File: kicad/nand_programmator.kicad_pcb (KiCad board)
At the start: 2 copper layers, 48 x 41 mm, 42 parts, among them J1 Conn_01x04, J2 Conn_01x03, J3 Conn_02x12_Odd_Even_Left, J4 Conn_02x12_Odd_Even_Right, J5 BOOT0, J6 ~RST, P1 USB, U1 LM1117-3.3, U2 STM32F103VCT6, Y1 Crystal_SMD_8MHz_18pF

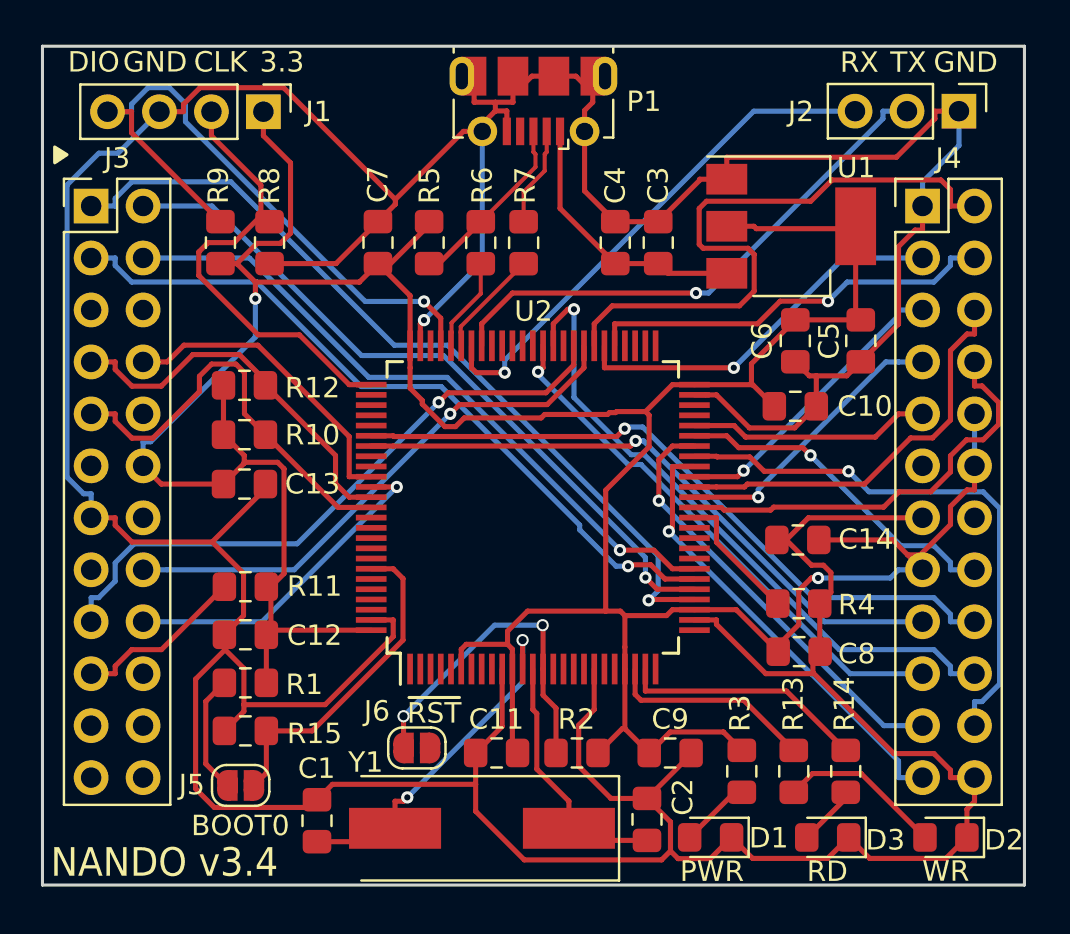
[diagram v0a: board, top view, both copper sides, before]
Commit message: Routed SPi tracks, added RST jumper
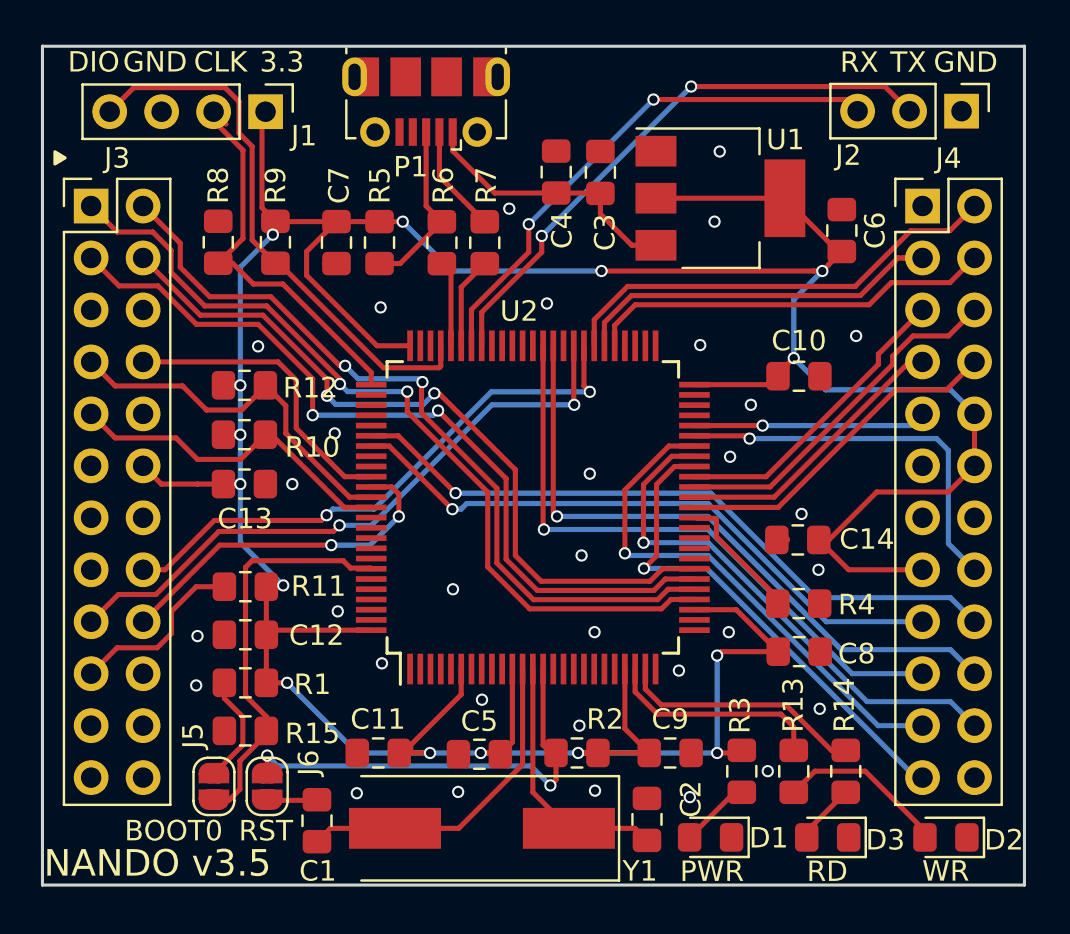
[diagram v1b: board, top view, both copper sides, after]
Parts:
- moved C5 27.5 mm to (189.2, 79.2), turned to 180 degrees
- moved J6 7.55 mm to (178.9, 80.8), turned to 90 degrees
- moved C6 5.85 mm to (206.9, 53.6), turned to 90 degrees
- moved C11 5.79 mm to (184.3, 79.2)
- moved P1 5.25 mm to (186.6, 47.4)
- moved C4 4.50 mm to (193.0, 50.8)
- moved C3 4.45 mm to (195.1, 50.8)
- moved U1 3.72 mm to (201.0, 52.1)
- moved R9 2.69 mm to (179.3, 54.2), turned to 270 degrees
- moved R8 2.51 mm to (176.5, 54.2), turned to 270 degrees
- moved R5 2.42 mm to (184.3, 54.2)
- moved C7 2.03 mm to (182.2, 54.2), turned to 270 degrees
- moved R7 1.90 mm to (189.5, 54.2)
- moved R6 1.90 mm to (187.4, 54.2)
- moved C10 1.48 mm to (204.9, 60.8)
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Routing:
- net GNDD: track 270.6 -> 3.56 mm, vias 1 -> 32
- net /FSMC_D15: track 31.0 -> 22.2 mm
- net +3V3: track 179.4 -> 185.9 mm, vias 2 -> 15
- net /SWDIO: track 31.9 -> 27.0 mm, vias 1 -> 0
- net /NRST: track 16.8 -> 21.3 mm
- net /FSMC_D4: track 20.9 -> 16.6 mm
- net /FSMC_D1: track 26.4 -> 30.4 mm
- net /FSMC_D10: track 21.5 -> 25.4 mm
- net /SPI1_MOSI: track 33.2 -> 37.1 mm, vias 1 -> 2
- net /FSMC_NCE2: track 20.4 -> 16.6 mm
- net /SPI1_SCK: track 35.3 -> 38.9 mm, vias 1 -> 2
- net /SPI1_MISO: track 36.4 -> 40.0 mm, vias 1 -> 2
- net /BOOT0: track 16.2 -> 19.7 mm
- net /SWCLK: track 22.2 -> 19.3 mm
- net /FSMC_D11: track 16.6 -> 19.1 mm
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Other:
- board text added: "NANDO v3.5"
- board text added: "RST"
- board text removed: "NANDO v3.4"
